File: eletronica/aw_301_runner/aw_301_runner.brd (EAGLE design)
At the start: 50.5 x 50.8 mm, 8 parts, among them IC1 ATTINY2313V, T1 2N2222

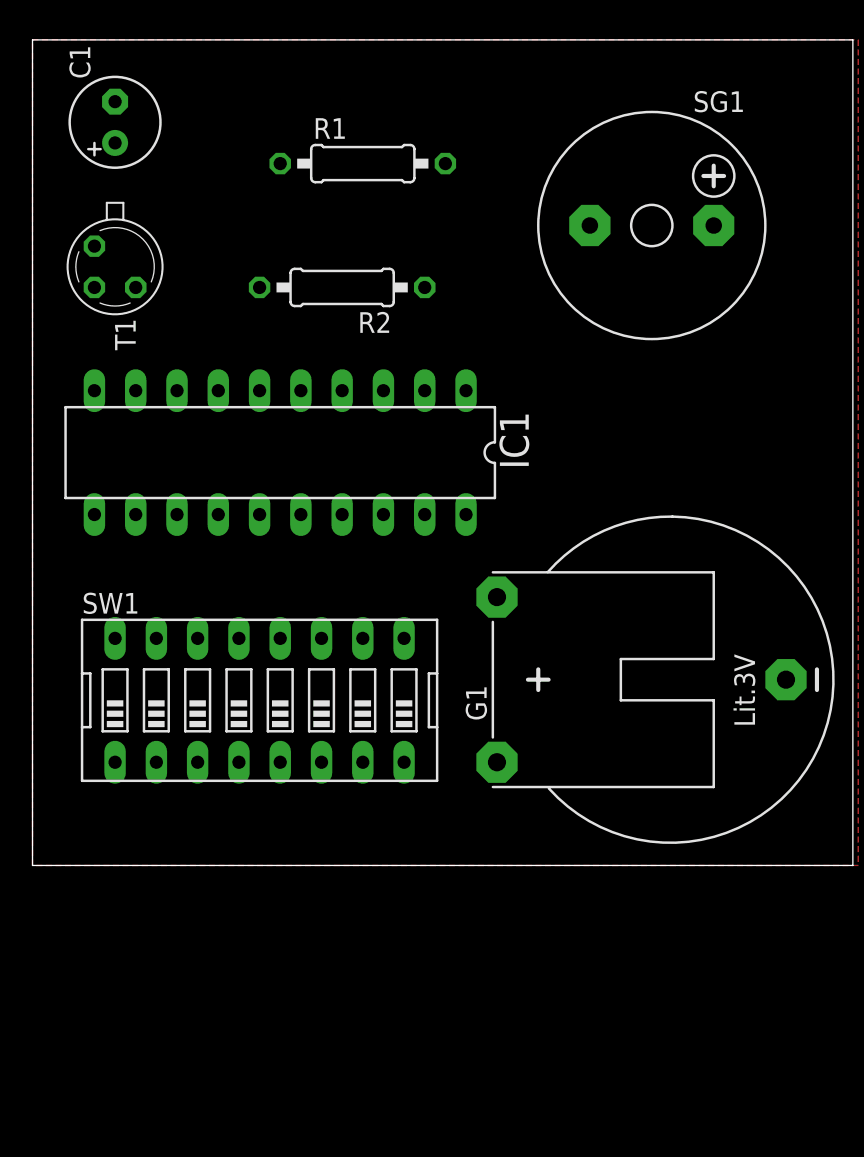
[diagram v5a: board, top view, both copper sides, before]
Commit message: 
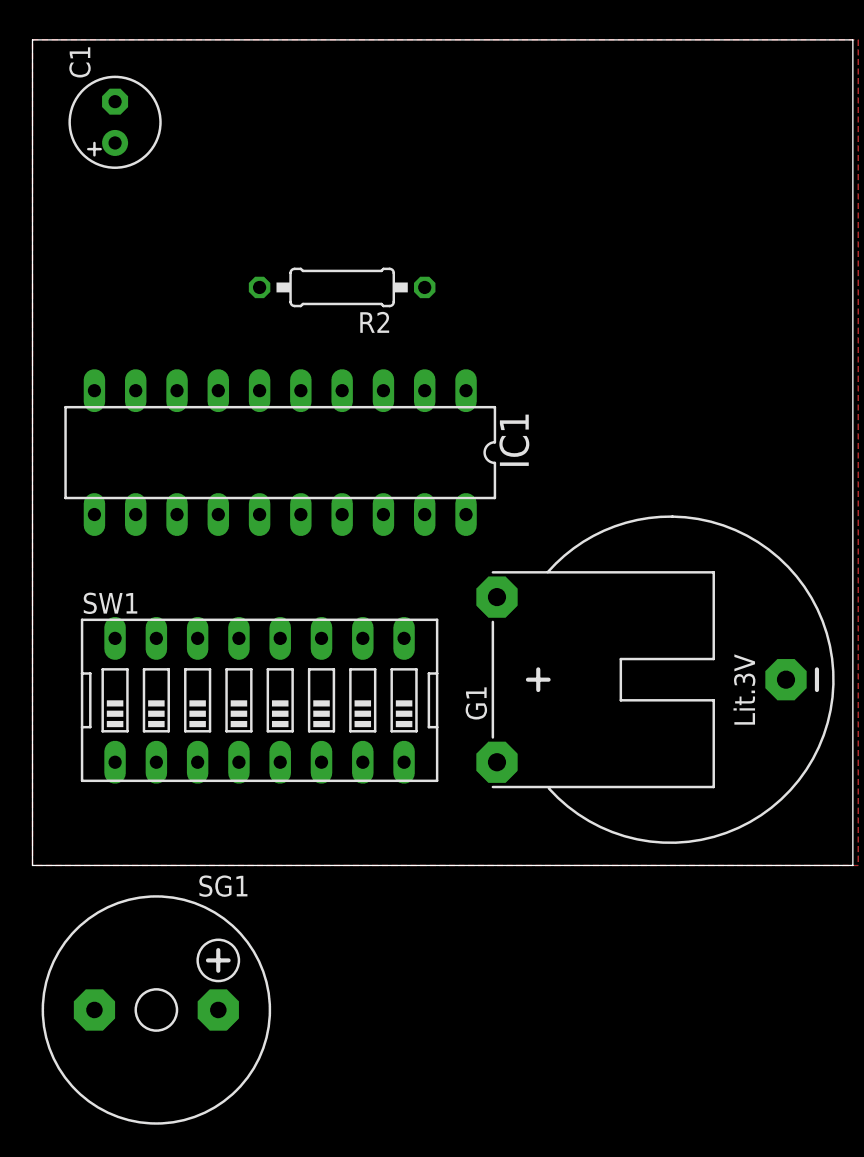
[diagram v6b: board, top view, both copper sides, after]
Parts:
- removed R1: ?, rcl:0207/10
- removed T1: 2N2222, transistor:TO18
- R2: value ? -> 50
- moved SG1 57.1 mm to (7.62, -8.89)
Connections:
- removed net N$1: SW1.1, SW1.2, SW1.3, SW1.4, SW1.5, SW1.6, SW1.7, SW1.8
- removed net N$4: R1.2, SG1.-, T1.3
- net GND: now also SG1.-; no longer IC1.1, T1.1
- net N$3: now also SG1.+; no longer T1.2
- net VCC: now also IC1.1, SW1.1, SW1.2, SW1.3, SW1.4, SW1.5, SW1.6, SW1.7, SW1.8; no longer R1.1, SG1.+
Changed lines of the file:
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@@
 <element name="SW1" library="special" package="EDG-08" value="" x="13.97" y="10.16"/>
 <element name="G1" library="battery" package="CR2032H" value="CR2032H" x="39.37" y="11.43" rot="R90"/>
-<element name="SG1" library="buzzer" package="F/CM12P" value="F/CM12P" x="38.1" y="39.37">
-<attribute name="OC_NEWARK" value="unknown" x="78.74" y="31.75" size="1.778" layer="27" display="off"/>
-<attribute name="MPN" value="" x="78.74" y="31.75" size="1.778" layer="27" display="off"/>
-<attribute name="MF" value="" x="78.74" y="31.75" size="1.778" layer="27" display="off"/>
-<attribute name="OC_FARNELL" value="unknown" x="78.74" y="31.75" size="1.778" layer="27" display="off"/>
+<element name="C1" library="resistor" package="E2,5-6" value="100mF" x="5.08" y="45.72" rot="R90"/>
+<element name="R2" library="rcl" package="0207/10" value="50" x="19.05" y="35.56" rot="R180"/>
+<element name="SG1" library="buzzer" package="F/CM12P" value="F/CM12P" x="7.62" y="-8.89">
+<attribute name="OC_NEWARK" value="unknown" x="7.62" y="-8.89" size="1.778" layer="27" display="off"/>
+<attribute name="MPN" value="" x="7.62" y="-8.89" size="1.778" layer="27" display="off"/>
+<attribute name="MF" value="" x="7.62" y="-8.89" size="1.778" layer="27" display="off"/>
+<attribute name="OC_FARNELL" value="unknown" x="7.62" y="-8.89" size="1.778" layer="27" display="off"/>
 </element>
-<element name="C1" library="resistor" package="E2,5-6" value="100mF" x="5.08" y="45.72" rot="R90"/>
-<element name="R2" library="rcl" package="0207/10" value="?" x="19.05" y="35.56" rot="R180"/>
-<element name="T1" library="transistor" package="TO18" value="2N2222" x="5.08" y="36.83" rot="R270"/>
-<element name="R1" library="rcl" package="0207/10" value="?" x="20.32" y="43.18"/>
 </elements>
 <signals>
 <signal name="VCC">
-<contactref element="R1" pad="1"/>
-<contactref element="SG1" pad="+"/>
 <contactref element="IC1" pad="20"/>
 <contactref element="C1" pad="+"/>
-<wire x1="26.67" y1="21.59" x2="41.91" y2="39.37" width="0" layer="19" extent="1-1"/>
-<wire x1="15.24" y1="43.18" x2="26.67" y2="21.59" width="0" layer="19" extent="1-1"/>
-<wire x1="5.08" y1="44.45" x2="15.24" y2="43.18" width="0" layer="19" extent="1-1"/>
+<contactref element="SW1" pad="8"/>
+<contactref element="SW1" pad="1"/>
+<contactref element="SW1" pad="2"/>
+<contactref element="SW1" pad="3"/>
+<contactref element="SW1" pad="4"/>
+<contactref element="SW1" pad="5"/>
+<contactref element="SW1" pad="6"/>
+<contactref element="SW1" pad="7"/>
+<contactref element="IC1" pad="1"/>
+<wire x1="26.67" y1="21.59" x2="26.67" y2="29.21" width="0" layer="19" extent="1-1"/>
+<wire x1="22.86" y1="6.35" x2="26.67" y2="21.59" width="0" layer="19" extent="1-1"/>
+<wire x1="20.32" y1="6.35" x2="22.86" y2="6.35" width="0" layer="19" extent="1-1"/>
+<wire x1="17.78" y1="6.35" x2="20.32" y2="6.35" width="0" layer="19" extent="1-1"/>
+<wire x1="15.24" y1="6.35" x2="17.78" y2="6.35" width="0" layer="19" extent="1-1"/>
+<wire x1="12.7" y1="6.35" x2="15.24" y2="6.35" width="0" layer="19" extent="1-1"/>
+<wire x1="10.16" y1="6.35" x2="12.7" y2="6.35" width="0" layer="19" extent="1-1"/>
+<wire x1="7.62" y1="6.35" x2="10.16" y2="6.35" width="0" layer="19" extent="1-1"/>
+<wire x1="5.08" y1="6.35" x2="7.62" y2="6.35" width="0" layer="19" extent="1-1"/>
+<wire x1="5.08" y1="44.45" x2="26.67" y2="29.21" width="0" layer="19" extent="1-1"/>
 </signal>
 <signal name="GND">
-<contactref element="T1" pad="1"/>
 <contactref element="G1" pad="-"/>
 <contactref element="C1" pad="-"/>
 <contactref element="IC1" pad="10"/>
-<contactref element="IC1" pad="1"/>
-<wire x1="26.67" y1="29.21" x2="46.355" y2="11.43" width="0" layer="19" extent="1-1"/>
-<wire x1="3.81" y1="29.21" x2="26.67" y2="29.21" width="0" layer="19" extent="1-1"/>
-<wire x1="3.81" y1="38.1" x2="3.81" y2="29.21" width="0" layer="19" extent="1-1"/>
-<wire x1="5.08" y1="46.99" x2="3.81" y2="38.1" width="0" layer="19" extent="1-1"/>
+<contactref element="SG1" pad="-"/>
+<wire x1="3.81" y1="29.21" x2="46.355" y2="11.43" width="0" layer="19" extent="1-1"/>
+<wire x1="5.08" y1="46.99" x2="3.81" y2="29.21" width="0" layer="19" extent="1-1"/>
+<wire x1="3.81" y1="-8.89" x2="3.81" y2="29.21" width="0" layer="19" extent="1-1"/>
 </signal>
 <signal name="N$8">
@@
 <wire x1="6.35" y1="29.21" x2="13.97" y2="35.56" width="0" layer="19" extent="1-1"/>
 </signal>
-<signal name="N$3">
-<contactref element="R2" pad="1"/>
-<contactref element="T1" pad="2"/>
-<wire x1="3.81" y1="35.56" x2="24.13" y2="35.56" width="0" layer="19" extent="1-1"/>
-</signal>
-<signal name="N$4">
-<contactref element="T1" pad="3"/>
-<contactref element="R1" pad="2"/>
-<contactref element="SG1" pad="-"/>
-<wire x1="25.4" y1="43.18" x2="34.29" y2="39.37" width="0" layer="19" extent="1-1"/>
-<wire x1="6.35" y1="35.56" x2="25.4" y2="43.18" width="0" layer="19" extent="1-1"/>
-</signal>
-<signal name="N$1">
-<contactref element="SW1" pad="8"/>
-<contactref element="SW1" pad="1"/>
-<contactref element="SW1" pad="2"/>
-<contactref element="SW1" pad="3"/>
-<contactref element="SW1" pad="4"/>
-<contactref element="SW1" pad="5"/>
-<contactref element="SW1" pad="6"/>
-<contactref element="SW1" pad="7"/>
-<wire x1="20.32" y1="6.35" x2="22.86" y2="6.35" width="0" layer="19" extent="1-1"/>
-<wire x1="17.78" y1="6.35" x2="20.32" y2="6.35" width="0" layer="19" extent="1-1"/>
-<wire x1="15.24" y1="6.35" x2="17.78" y2="6.35" width="0" layer="19" extent="1-1"/>
-<wire x1="12.7" y1="6.35" x2="15.24" y2="6.35" width="0" layer="19" extent="1-1"/>
-<wire x1="10.16" y1="6.35" x2="12.7" y2="6.35" width="0" layer="19" extent="1-1"/>
-<wire x1="7.62" y1="6.35" x2="10.16" y2="6.35" width="0" layer="19" extent="1-1"/>
-<wire x1="5.08" y1="6.35" x2="7.62" y2="6.35" width="0" layer="19" extent="1-1"/>
-</signal>
 <signal name="N$5">
 <contactref element="G1" pad="+"/>
@@
 </polygon>
 </signal>
+<signal name="N$3">
+<contactref element="R2" pad="1"/>
+<contactref element="SG1" pad="+"/>
+<wire x1="11.43" y1="-8.89" x2="24.13" y2="35.56" width="0" layer="19" extent="1-1"/>
+</signal>
 </signals>

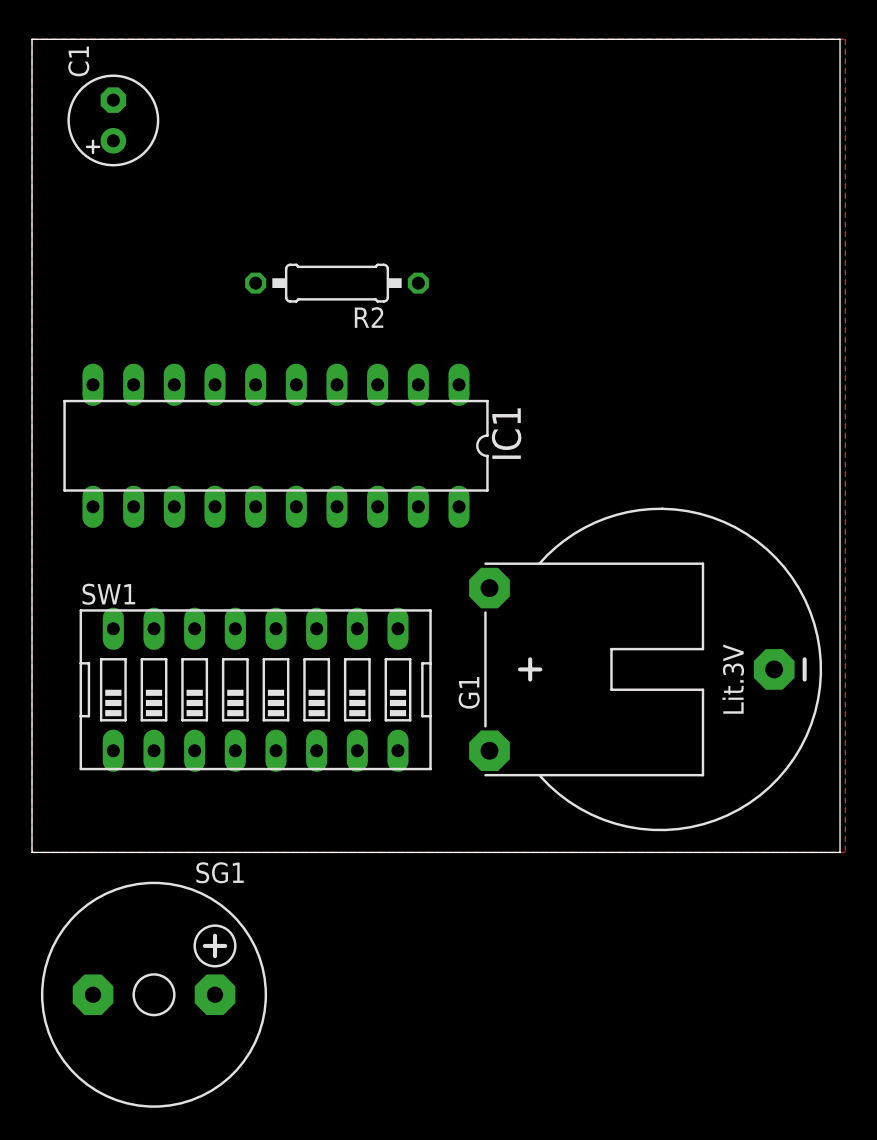
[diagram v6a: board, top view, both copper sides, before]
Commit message: 
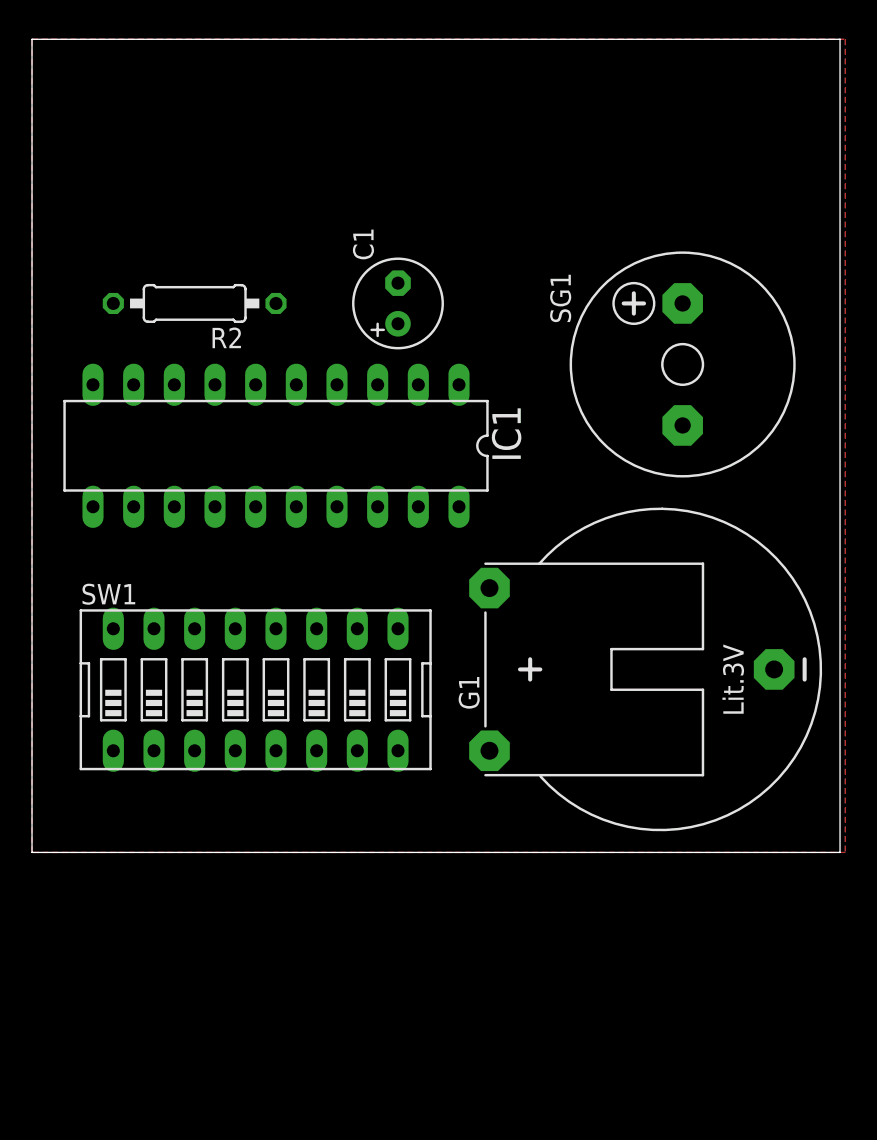
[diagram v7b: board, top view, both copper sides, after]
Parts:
- moved SG1 51.4 mm to (40.6, 30.5), turned to 90 degrees
- moved C1 21.1 mm to (22.9, 34.3)
- moved R2 8.98 mm to (10.2, 34.3)
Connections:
- net GND: now also SW1.1, SW1.2, SW1.3, SW1.4, SW1.5, SW1.6, SW1.7
- net N$5: now also C1.+, IC1.1, IC1.20; no longer G1.+
- net VCC: now also G1.+; no longer C1.+, IC1.1, IC1.20, SW1.1, SW1.2, SW1.3, SW1.4, SW1.5, SW1.6, SW1.7
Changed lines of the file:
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@@
 <element name="SW1" library="special" package="EDG-08" value="" x="13.97" y="10.16"/>
 <element name="G1" library="battery" package="CR2032H" value="CR2032H" x="39.37" y="11.43" rot="R90"/>
-<element name="C1" library="resistor" package="E2,5-6" value="100mF" x="5.08" y="45.72" rot="R90"/>
-<element name="R2" library="rcl" package="0207/10" value="50" x="19.05" y="35.56" rot="R180"/>
-<element name="SG1" library="buzzer" package="F/CM12P" value="F/CM12P" x="7.62" y="-8.89">
-<attribute name="OC_NEWARK" value="unknown" x="7.62" y="-8.89" size="1.778" layer="27" display="off"/>
-<attribute name="MPN" value="" x="7.62" y="-8.89" size="1.778" layer="27" display="off"/>
-<attribute name="MF" value="" x="7.62" y="-8.89" size="1.778" layer="27" display="off"/>
-<attribute name="OC_FARNELL" value="unknown" x="7.62" y="-8.89" size="1.778" layer="27" display="off"/>
+<element name="C1" library="resistor" package="E2,5-6" value="100mF" x="22.86" y="34.29" rot="R90"/>
+<element name="R2" library="rcl" package="0207/10" value="50" x="10.16" y="34.29" rot="R180"/>
+<element name="SG1" library="buzzer" package="F/CM12P" value="F/CM12P" x="40.64" y="30.48" rot="R90">
+<attribute name="OC_NEWARK" value="unknown" x="40.64" y="30.48" size="1.778" layer="27" rot="R90" display="off"/>
+<attribute name="MPN" value="" x="40.64" y="30.48" size="1.778" layer="27" rot="R90" display="off"/>
+<attribute name="MF" value="" x="40.64" y="30.48" size="1.778" layer="27" rot="R90" display="off"/>
+<attribute name="OC_FARNELL" value="unknown" x="40.64" y="30.48" size="1.778" layer="27" rot="R90" display="off"/>
 </element>
 </elements>
 <signals>
-<signal name="VCC">
-<contactref element="IC1" pad="20"/>
-<contactref element="C1" pad="+"/>
-<contactref element="SW1" pad="8"/>
+<signal name="GND">
+<contactref element="G1" pad="-"/>
+<contactref element="C1" pad="-"/>
+<contactref element="IC1" pad="10"/>
+<contactref element="SG1" pad="-"/>
 <contactref element="SW1" pad="1"/>
 <contactref element="SW1" pad="2"/>
@@
 <contactref element="SW1" pad="6"/>
 <contactref element="SW1" pad="7"/>
-<contactref element="IC1" pad="1"/>
-<wire x1="26.67" y1="21.59" x2="26.67" y2="29.21" width="0" layer="19" extent="1-1"/>
-<wire x1="22.86" y1="6.35" x2="26.67" y2="21.59" width="0" layer="19" extent="1-1"/>
-<wire x1="20.32" y1="6.35" x2="22.86" y2="6.35" width="0" layer="19" extent="1-1"/>
+<wire x1="20.32" y1="6.35" x2="46.355" y2="11.43" width="0" layer="19" extent="1-1"/>
 <wire x1="17.78" y1="6.35" x2="20.32" y2="6.35" width="0" layer="19" extent="1-1"/>
 <wire x1="15.24" y1="6.35" x2="17.78" y2="6.35" width="0" layer="19" extent="1-1"/>
@@
 <wire x1="7.62" y1="6.35" x2="10.16" y2="6.35" width="0" layer="19" extent="1-1"/>
 <wire x1="5.08" y1="6.35" x2="7.62" y2="6.35" width="0" layer="19" extent="1-1"/>
-<wire x1="5.08" y1="44.45" x2="26.67" y2="29.21" width="0" layer="19" extent="1-1"/>
-</signal>
-<signal name="GND">
-<contactref element="G1" pad="-"/>
-<contactref element="C1" pad="-"/>
-<contactref element="IC1" pad="10"/>
-<contactref element="SG1" pad="-"/>
-<wire x1="3.81" y1="29.21" x2="46.355" y2="11.43" width="0" layer="19" extent="1-1"/>
-<wire x1="5.08" y1="46.99" x2="3.81" y2="29.21" width="0" layer="19" extent="1-1"/>
-<wire x1="3.81" y1="-8.89" x2="3.81" y2="29.21" width="0" layer="19" extent="1-1"/>
-</signal>
-<signal name="N$8">
-<contactref element="SW1" pad="16"/>
-<contactref element="IC1" pad="12"/>
-<wire x1="5.08" y1="13.97" x2="6.35" y2="21.59" width="0" layer="19" extent="1-1"/>
-</signal>
-<signal name="N$9">
-<contactref element="SW1" pad="15"/>
-<contactref element="IC1" pad="13"/>
-<wire x1="7.62" y1="13.97" x2="8.89" y2="21.59" width="0" layer="19" extent="1-1"/>
-</signal>
-<signal name="N$10">
-<contactref element="SW1" pad="14"/>
-<contactref element="IC1" pad="14"/>
-<wire x1="10.16" y1="13.97" x2="11.43" y2="21.59" width="0" layer="19" extent="1-1"/>
-</signal>
-<signal name="N$11">
-<contactref element="SW1" pad="13"/>
-<contactref element="IC1" pad="15"/>
-<wire x1="12.7" y1="13.97" x2="13.97" y2="21.59" width="0" layer="19" extent="1-1"/>
-</signal>
-<signal name="N$12">
-<contactref element="SW1" pad="12"/>
-<contactref element="IC1" pad="16"/>
-<wire x1="15.24" y1="13.97" x2="16.51" y2="21.59" width="0" layer="19" extent="1-1"/>
-</signal>
-<signal name="N$13">
-<contactref element="SW1" pad="11"/>
-<contactref element="IC1" pad="17"/>
-<wire x1="17.78" y1="13.97" x2="19.05" y2="21.59" width="0" layer="19" extent="1-1"/>
-</signal>
-<signal name="N$14">
-<contactref element="SW1" pad="10"/>
-<contactref element="IC1" pad="18"/>
-<wire x1="20.32" y1="13.97" x2="21.59" y2="21.59" width="0" layer="19" extent="1-1"/>
+<wire x1="40.64" y1="26.67" x2="5.08" y2="6.35" width="0" layer="19" extent="1-1"/>
+<wire x1="3.81" y1="29.21" x2="5.08" y2="6.35" width="0" layer="19" extent="1-1"/>
+<wire x1="22.86" y1="35.56" x2="3.81" y2="29.21" width="0" layer="19" extent="1-1"/>
 </signal>
 <signal name="N$2">
 <contactref element="IC1" pad="9"/>
 <contactref element="R2" pad="2"/>
-<wire x1="6.35" y1="29.21" x2="13.97" y2="35.56" width="0" layer="19" extent="1-1"/>
-</signal>
-<signal name="N$5">
-<contactref element="G1" pad="+"/>
-<contactref element="SW1" pad="9"/>
-<wire x1="22.86" y1="13.97" x2="28.575" y2="16.51" width="0" layer="19" extent="1-1"/>
+<wire x1="6.35" y1="29.21" x2="5.08" y2="34.29" width="0" layer="19" extent="1-1"/>
 </signal>
 <signal name="N$6">
@@
 <contactref element="R2" pad="1"/>
 <contactref element="SG1" pad="+"/>
-<wire x1="11.43" y1="-8.89" x2="24.13" y2="35.56" width="0" layer="19" extent="1-1"/>
+<wire x1="40.64" y1="34.29" x2="15.24" y2="34.29" width="0" layer="19" extent="1-1"/>
+</signal>
+<signal name="VCC">
+<contactref element="G1" pad="+"/>
+<contactref element="SW1" pad="8"/>
+<wire x1="22.86" y1="6.35" x2="28.575" y2="16.51" width="0" layer="19" extent="1-1"/>
+</signal>
+<signal name="N$5">
+<contactref element="SW1" pad="9"/>
+<contactref element="IC1" pad="20"/>
+<contactref element="C1" pad="+"/>
+<contactref element="IC1" pad="1"/>
+<wire x1="26.67" y1="21.59" x2="26.67" y2="29.21" width="0" layer="19" extent="1-1"/>
+<wire x1="22.86" y1="13.97" x2="26.67" y2="21.59" width="0" layer="19" extent="1-1"/>
+<wire x1="22.86" y1="33.02" x2="26.67" y2="29.21" width="0" layer="19" extent="1-1"/>
+</signal>
+<signal name="N$4">
+<contactref element="IC1" pad="12"/>
+<contactref element="SW1" pad="16"/>
+<wire x1="5.08" y1="13.97" x2="6.35" y2="21.59" width="0" layer="19" extent="1-1"/>
+</signal>
+<signal name="N$7">
+<contactref element="IC1" pad="13"/>
+<contactref element="SW1" pad="15"/>
+<wire x1="7.62" y1="13.97" x2="8.89" y2="21.59" width="0" layer="19" extent="1-1"/>
+</signal>
+<signal name="N$8">
+<contactref element="IC1" pad="14"/>
+<contactref element="SW1" pad="14"/>
+<wire x1="10.16" y1="13.97" x2="11.43" y2="21.59" width="0" layer="19" extent="1-1"/>
+</signal>
+<signal name="N$9">
+<contactref element="IC1" pad="15"/>
+<contactref element="SW1" pad="13"/>
+<wire x1="12.7" y1="13.97" x2="13.97" y2="21.59" width="0" layer="19" extent="1-1"/>
+</signal>
+<signal name="N$10">
+<contactref element="IC1" pad="16"/>
+<contactref element="SW1" pad="12"/>
+<wire x1="15.24" y1="13.97" x2="16.51" y2="21.59" width="0" layer="19" extent="1-1"/>
+</signal>
+<signal name="N$11">
+<contactref element="IC1" pad="17"/>
+<contactref element="SW1" pad="11"/>
+<wire x1="17.78" y1="13.97" x2="19.05" y2="21.59" width="0" layer="19" extent="1-1"/>
+</signal>
+<signal name="N$12">
+<contactref element="IC1" pad="18"/>
+<contactref element="SW1" pad="10"/>
+<wire x1="20.32" y1="13.97" x2="21.59" y2="21.59" width="0" layer="19" extent="1-1"/>
 </signal>
 </signals>
